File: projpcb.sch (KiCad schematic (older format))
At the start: 21 parts, among them CON1 BARREL_JACK, CON2 BARREL_JACK, P1 CONN_01X02, P2 CONN_01X02, P3 CONN_02X05, P4 CONN_02X05, Q16 Q_NMOS_GSD, U1 Teensy_3.1, U2 LM358, U3 CD74HC4067, U4 CL520

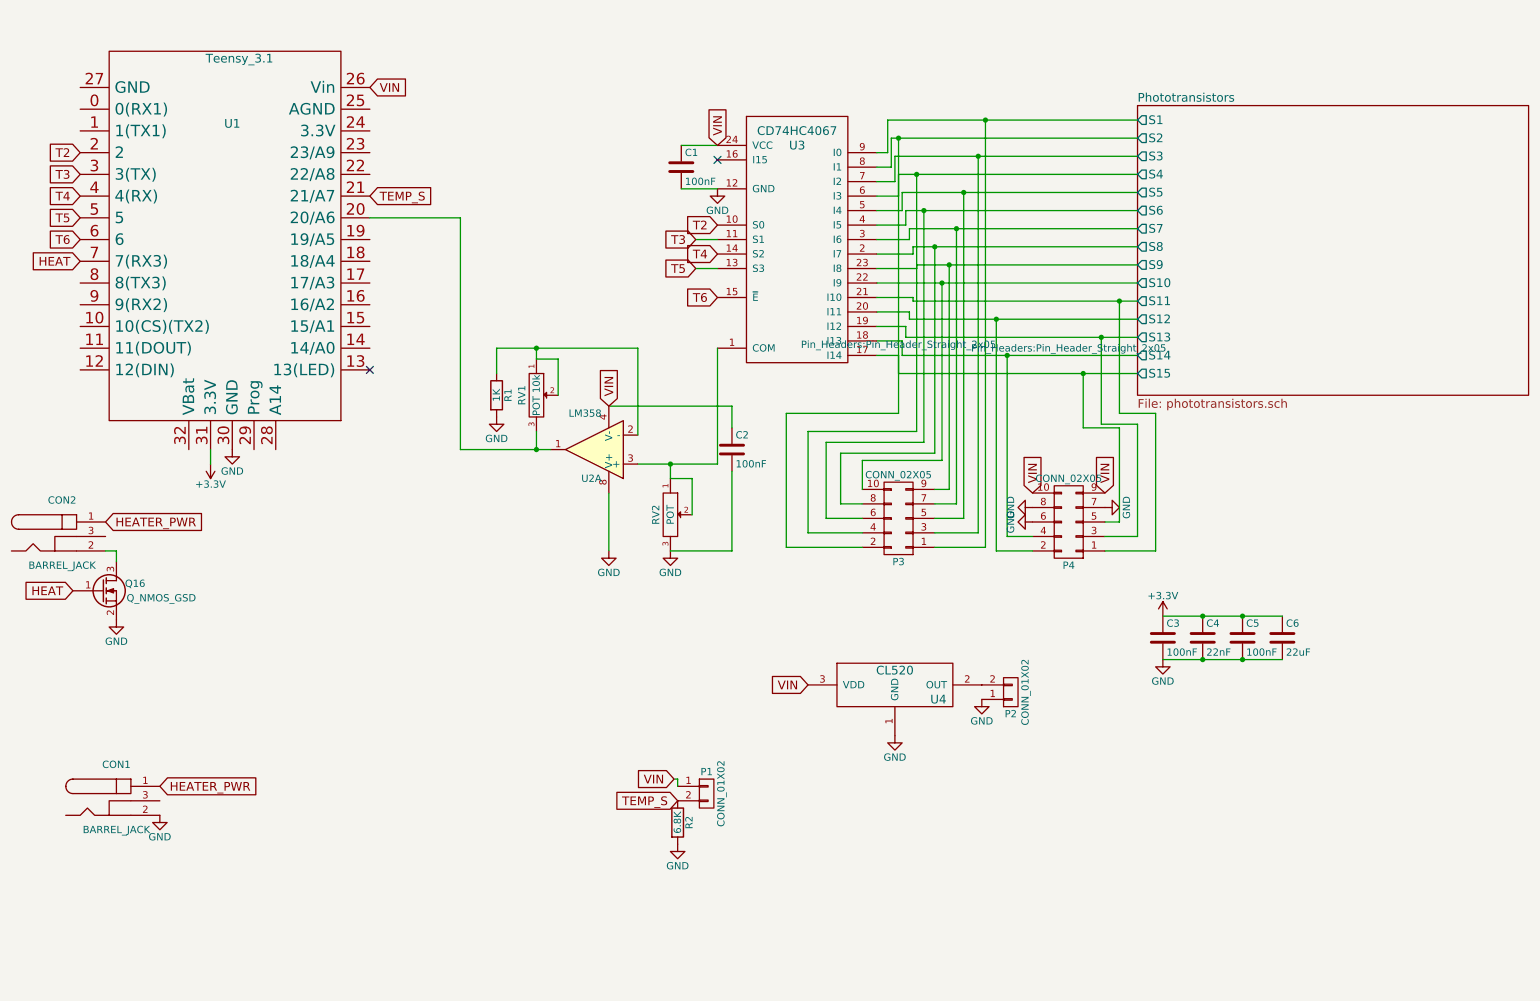
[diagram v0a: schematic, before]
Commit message: Changed VIN --> 3.3v, analog GND to AGND, added 3 status LED's
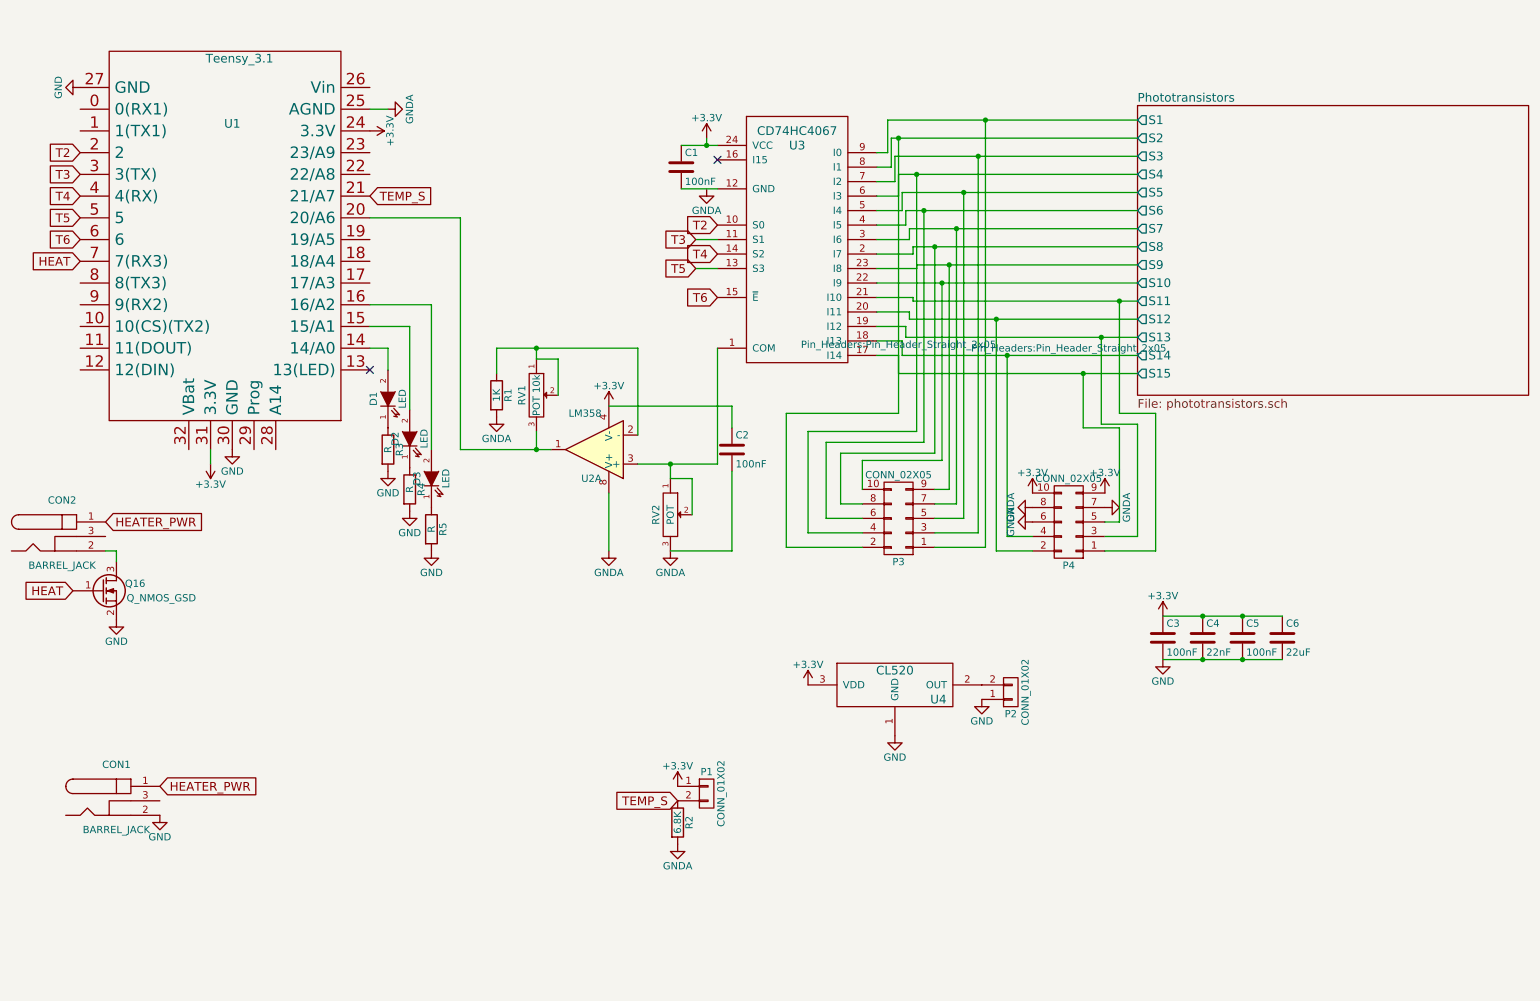
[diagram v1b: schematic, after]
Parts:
- added D1, D2, D3: LED, LEDs:LED_0805, symbol LED
- added R3, R4, R5: R, Resistors_SMD:R_0805_HandSoldering, symbol R
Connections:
- net +3V3: now also C1.1, C2.1, P1.1 (P1), P4.10 (P10), P4.9 (P9), U1.24 (3.3V), U2.4 (V-), U3.24 (VCC), U4.3 (VDD)
- net GND: now also U1.27 (GND), R3.2, R4.2, R5.2; no longer C1.2, C2.2, P4.6 (P6), P4.7 (P7), P4.8 (P8), R1.2, R2.2, RV2.3, U2.8 (V+), U3.12 (GND)
- net at U1.14 (14/A0): now also D1.2 (A)
- net at U1.15 (15/A1): now also D2.2 (A)
- net at U1.16 (16/A2): now also D3.2 (A)
- net GNDA: now reaches U1.25 (AGND)
- net GNDA: now also C2.2, P4.6 (P6), P4.7 (P7), P4.8 (P8), R1.2, R2.2, RV2.3, U2.8 (V+)
- removed net VIN: C1.1, C2.1, P1.1 (P1), P4.10 (P10), P4.9 (P9), U1.26 (Vin), U2.4 (V-), U3.24 (VCC), U4.3 (VDD)
- new net: C1.2, U3.12 (GND)
- new net: D1.1 (K), R3.1
- new net: D2.1 (K), R4.1
- new net: D3.1 (K), R5.1

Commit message: PCB
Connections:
- net GNDA: now also C1.2, U3.12 (GND)
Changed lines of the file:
@@
 L GNDA #PWR17
 U 1 1 56C8B94A
-P 5350 1850
-F 0 "#PWR17" H 5350 1600 50  0001 C CNN
-F 1 "GNDA" H 5350 1700 50  0000 C CNN
-F 2 "" H 5350 1850 50  0000 C CNN
-F 3 "" H 5350 1850 50  0000 C CNN
-	1    5350 1850
+P 5350 1875
+F 0 "#PWR17" H 5350 1625 50  0001 C CNN
+F 1 "GNDA" H 5350 1725 50  0000 C CNN
+F 2 "" H 5350 1875 50  0000 C CNN
+F 3 "" H 5350 1875 50  0000 C CNN
+	1    5350 1875
 	1    0    0    -1
 $EndComp
@@
 	0    1    1    0
 $EndComp
+Wire Wire Line
+	5350 1875 5350 1850
+Connection ~ 5350 1850
 $EndSCHEMATC

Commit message: VERSION ONE - Sent for manufacturegit add -Agit add -A
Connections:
- net GNDA is gone; now on net GND: C1.2, C2.2, P4.6 (P6), P4.7 (P7), P4.8 (P8), R1.2, R2.2, RV2.3, U1.25 (AGND), U2.8 (V+), U3.12 (GND)
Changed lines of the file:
@@
 	1    0    0    -1
-$EndComp
-$Comp
-L GNDA #PWR6
-U 1 1 56C8B60B
-P 3150 1300
-F 0 "#PWR6" H 3150 1050 50  0001 C CNN
-F 1 "GNDA" H 3150 1150 50  0000 C CNN
-F 2 "" H 3150 1300 50  0000 C CNN
-F 3 "" H 3150 1300 50  0000 C CNN
-	1    3150 1300
-	0    -1   -1   0
-$EndComp
-$Comp
-L GNDA #PWR17
-U 1 1 56C8B94A
-P 5350 1875
-F 0 "#PWR17" H 5350 1625 50  0001 C CNN
-F 1 "GNDA" H 5350 1725 50  0000 C CNN
-F 2 "" H 5350 1875 50  0000 C CNN
-F 3 "" H 5350 1875 50  0000 C CNN
-	1    5350 1875
-	1    0    0    -1
-$EndComp
-$Comp
-L GNDA #PWR13
-U 1 1 56C8C123
-P 5100 4350
-F 0 "#PWR13" H 5100 4100 50  0001 C CNN
-F 1 "GNDA" H 5100 4200 50  0000 C CNN
-F 2 "" H 5100 4350 50  0000 C CNN
-F 3 "" H 5100 4350 50  0000 C CNN
-	1    5100 4350
-	1    0    0    -1
-$EndComp
-$Comp
-L GNDA #PWR12
-U 1 1 56C8C45B
-P 4675 4350
-F 0 "#PWR12" H 4675 4100 50  0001 C CNN
-F 1 "GNDA" H 4675 4200 50  0000 C CNN
-F 2 "" H 4675 4350 50  0000 C CNN
-F 3 "" H 4675 4350 50  0000 C CNN
-	1    4675 4350
-	1    0    0    -1
-$EndComp
-$Comp
-L GNDA #PWR10
-U 1 1 56C8C4FF
-P 3900 3425
-F 0 "#PWR10" H 3900 3175 50  0001 C CNN
-F 1 "GNDA" H 3900 3275 50  0000 C CNN
-F 2 "" H 3900 3425 50  0000 C CNN
-F 3 "" H 3900 3425 50  0000 C CNN
-	1    3900 3425
-	1    0    0    -1
-$EndComp
-$Comp
-L GNDA #PWR22
-U 1 1 56C8CBFD
-P 7600 4050
-F 0 "#PWR22" H 7600 3800 50  0001 C CNN
-F 1 "GNDA" H 7600 3900 50  0000 C CNN
-F 2 "" H 7600 4050 50  0000 C CNN
-F 3 "" H 7600 4050 50  0000 C CNN
-	1    7600 4050
-	0    1    1    0
-$EndComp
-$Comp
-L GNDA #PWR23
-U 1 1 56C8CCA1
-P 7600 4150
-F 0 "#PWR23" H 7600 3900 50  0001 C CNN
-F 1 "GNDA" H 7600 4000 50  0000 C CNN
-F 2 "" H 7600 4150 50  0000 C CNN
-F 3 "" H 7600 4150 50  0000 C CNN
-	1    7600 4150
-	0    1    1    0
-$EndComp
-$Comp
-L GNDA #PWR25
-U 1 1 56C8CD45
-P 8100 4050
-F 0 "#PWR25" H 8100 3800 50  0001 C CNN
-F 1 "GNDA" H 8100 3900 50  0000 C CNN
-F 2 "" H 8100 4050 50  0000 C CNN
-F 3 "" H 8100 4050 50  0000 C CNN
-	1    8100 4050
-	0    -1   -1   0
 $EndComp
 Wire Wire Line
@@
 	3450 2650 3025 2650
 $Comp
-L GNDA #PWR15
-U 1 1 56C988D5
-P 5150 6375
-F 0 "#PWR15" H 5150 6125 50  0001 C CNN
-F 1 "GNDA" H 5150 6225 50  0000 C CNN
-F 2 "" H 5150 6375 50  0000 C CNN
-F 3 "" H 5150 6375 50  0000 C CNN
-	1    5150 6375
-	1    0    0    -1
-$EndComp
-$Comp
 L GND #PWR?
 U 1 1 56CD6885
@@
 	5350 1875 5350 1850
 Connection ~ 5350 1850
+$Comp
+L GND #PWR?
+U 1 1 56E2450E
+P 4675 4350
+F 0 "#PWR?" H 4675 4100 50  0001 C CNN
+F 1 "GND" H 4675 4200 50  0000 C CNN
+F 2 "" H 4675 4350 50  0000 C CNN
+F 3 "" H 4675 4350 50  0000 C CNN
+	1    4675 4350
+	1    0    0    -1
+$EndComp
+$Comp
+L GND #PWR?
+U 1 1 56E246E4
+P 5100 4350
+F 0 "#PWR?" H 5100 4100 50  0001 C CNN
+F 1 "GND" H 5100 4200 50  0000 C CNN
+F 2 "" H 5100 4350 50  0000 C CNN
+F 3 "" H 5100 4350 50  0000 C CNN
+	1    5100 4350
+	1    0    0    -1
+$EndComp
+$Comp
+L GND #PWR?
+U 1 1 56E24872
+P 3150 1300
+F 0 "#PWR?" H 3150 1050 50  0001 C CNN
+F 1 "GND" H 3150 1150 50  0000 C CNN
+F 2 "" H 3150 1300 50  0000 C CNN
+F 3 "" H 3150 1300 50  0000 C CNN
+	1    3150 1300
+	0    -1   -1   0
+$EndComp
+$Comp
+L GND #PWR?
+U 1 1 56E24F5B
+P 3900 3425
+F 0 "#PWR?" H 3900 3175 50  0001 C CNN
+F 1 "GND" H 3900 3275 50  0000 C CNN
+F 2 "" H 3900 3425 50  0000 C CNN
+F 3 "" H 3900 3425 50  0000 C CNN
+	1    3900 3425
+	1    0    0    -1
+$EndComp
+$Comp
+L GND #PWR?
+U 1 1 56E2557C
+P 5350 1875
+F 0 "#PWR?" H 5350 1625 50  0001 C CNN
+F 1 "GND" H 5350 1725 50  0000 C CNN
+F 2 "" H 5350 1875 50  0000 C CNN
+F 3 "" H 5350 1875 50  0000 C CNN
+	1    5350 1875
+	1    0    0    -1
+$EndComp
+$Comp
+L GND #PWR?
+U 1 1 56E25B03
+P 7600 4150
+F 0 "#PWR?" H 7600 3900 50  0001 C CNN
+F 1 "GND" H 7600 4000 50  0000 C CNN
+F 2 "" H 7600 4150 50  0000 C CNN
+F 3 "" H 7600 4150 50  0000 C CNN
+	1    7600 4150
+	0    1    1    0
+$EndComp
+$Comp
+L GND #PWR?
+U 1 1 56E25C49
+P 7600 4050
+F 0 "#PWR?" H 7600 3800 50  0001 C CNN
+F 1 "GND" H 7600 3900 50  0000 C CNN
+F 2 "" H 7600 4050 50  0000 C CNN
+F 3 "" H 7600 4050 50  0000 C CNN
+	1    7600 4050
+	0    1    1    0
+$EndComp
+$Comp
+L GND #PWR?
+U 1 1 56E25CFF
+P 8100 4050
+F 0 "#PWR?" H 8100 3800 50  0001 C CNN
+F 1 "GND" H 8100 3900 50  0000 C CNN
+F 2 "" H 8100 4050 50  0000 C CNN
+F 3 "" H 8100 4050 50  0000 C CNN
+	1    8100 4050
+	0    -1   -1   0
+$EndComp
+$Comp
+L GND #PWR?
+U 1 1 56E261BA
+P 5150 6375
+F 0 "#PWR?" H 5150 6125 50  0001 C CNN
+F 1 "GND" H 5150 6225 50  0000 C CNN
+F 2 "" H 5150 6375 50  0000 C CNN
+F 3 "" H 5150 6375 50  0000 C CNN
+	1    5150 6375
+	1    0    0    -1
+$EndComp
 $EndSCHEMATC

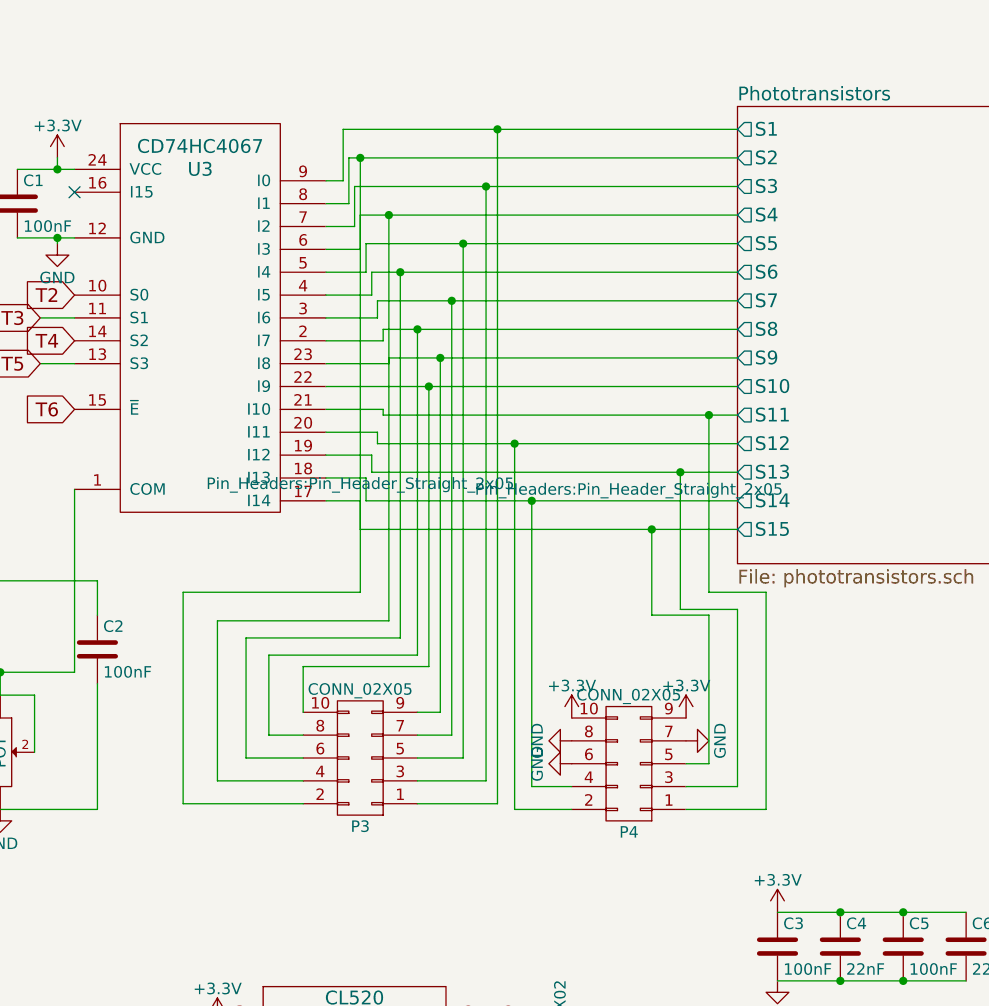
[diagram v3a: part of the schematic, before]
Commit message: Added missing pot, logos and mounting holes.
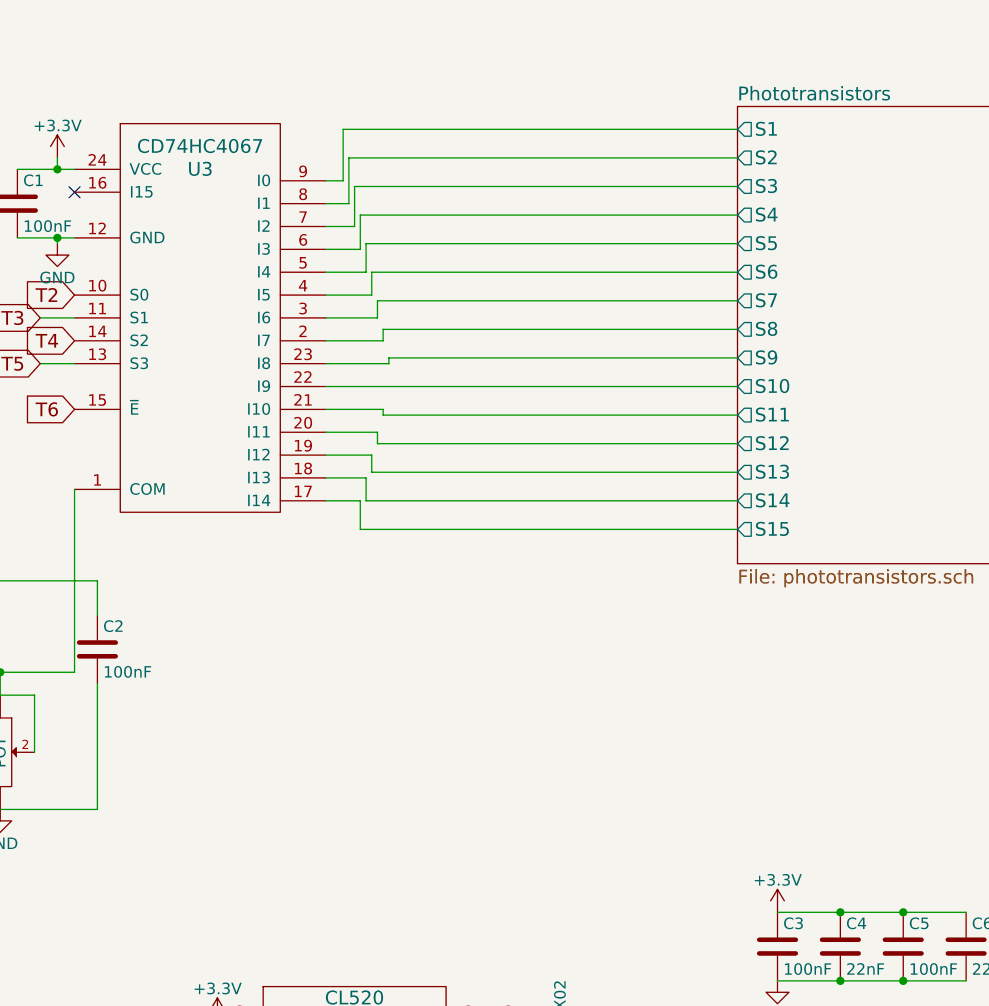
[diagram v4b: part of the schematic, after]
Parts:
- removed P3, P4: CONN_02X05, Pin_Headers:Pin_Header_Straight_2x05, symbol CONN_02X05
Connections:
- net Phototransistors/S15: no longer U3.23 (I8), U3.6 (I3), U3.8 (I1)
- new net Phototransistors/S2: U3.8 (I1)
- new net Phototransistors/S4: U3.6 (I3)
- new net Phototransistors/S9: U3.23 (I8)
